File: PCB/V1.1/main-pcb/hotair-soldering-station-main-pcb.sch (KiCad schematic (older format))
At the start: 83 parts, among them J1 230VAC_IN, J10 SOLD_IRON (r.2,54), J13 ICP (goldpin r2,54), J2 main-board-conn, J3 EARTH_GND, J4 24V_IN (NS-25 r2,54), J5 PSUPPLY (PWZ-02S r.3,96), J6 HOTAIR_FAN (JST r,2,54), J7 HOTAIR_MEAS (JST r.2,5), J8 HOTAIR_HEATER (PWZ-02S r.3,96)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

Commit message: Add front panel menu sw, remove lcd, reorganization of uC pinout
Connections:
- net labels added: HOTAIR_FAN_ADC, HOTAIR_FAN_PWM, HOTAIR_TEMP_ADC, IRON_T12_MOTION_SW, IRON_T12_TEMP_ADC, LCD_BACKLIGHT_PWM, LCD_D4, LCD_D5, LCD_D6, LCD_D7, LCD_EN, LCD_RS, LCD_RW, MENU_DOWN_SW, MENU_OK_SW, MENU_UP_SW, SOLDER_SELECT_SW
- net labels removed: 7SEG_LATCH, FAN_ADC, FAN_PWM, HOTAIR_ADC, IRON_T12_ADC
- wire segments 317 -> 324
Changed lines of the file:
@@
 Wire Wire Line
 	20125 2800 20125 2550
+Text GLabel 21150 3200 2    50   Input ~ 0
+HOTAIR_UP_SW
+Text GLabel 21150 3100 2    50   Input ~ 0
+HOTAIR_DOWN_SW
 Text GLabel 20150 3400 0    50   Input ~ 0
-HOTAIR_UP_SW
+SOLDER_UP_SW
 Text GLabel 20150 3300 0    50   Input ~ 0
-HOTAIR_DOWN_SW
-Text GLabel 20150 3200 0    50   Input ~ 0
-SOLDER_UP_SW
-Text GLabel 20150 3100 0    50   Input ~ 0
 SOLDER_DOWN_SW
-Text GLabel 21150 3200 2    50   Input ~ 0
+Text GLabel 21150 2900 2    50   Input ~ 0
 HOTAIR_ON_SW
-Text GLabel 21150 3100 2    50   Input ~ 0
+Text GLabel 21150 2800 2    50   Input ~ 0
 SOLDER_ON_SW
-Text GLabel 21150 2800 2    50   Input ~ 0
-SPI1_MOSI
-Text GLabel 21150 3000 2    50   Input ~ 0
-SPI1_SCK
-Text GLabel 21150 2900 2    50   Input ~ 0
-7SEG_LATCH
 Wire Notes Line
 	6475 11250 6425 11250
@@
 Wire Notes Line
 	12700 16075 12750 16075
-Text GLabel 18450 8950 2    50   Input ~ 0
-HOTAIR_UP_SW
-Text GLabel 16250 8550 0    50   Input ~ 0
-HOTAIR_DOWN_SW
-Text GLabel 18450 8850 2    50   Input ~ 0
-SPI1_MOSI
-Text GLabel 18450 8650 2    50   Input ~ 0
-SPI1_SCK
-Text GLabel 18450 8750 2    50   Input ~ 0
-SPI1_MISO
-Text GLabel 18450 8150 2    50   Input ~ 0
-IRON_T12_ADC
 $Comp
 L Device:R R18
@@
 $EndComp
 Text GLabel 5625 12050 2    50   Input ~ 0
-HOTAIR_ADC
-Text GLabel 18450 8250 2    50   Input ~ 0
-HOTAIR_ADC
+HOTAIR_TEMP_ADC
 Wire Notes Line
 	650  12850 6525 12850
@@
 	1    0    0    -1
 $EndComp
-Text GLabel 18450 9050 2    50   Input ~ 0
+Text GLabel 18450 9650 2    50   Input ~ 0
 UART_DBG_TX
 Wire Wire Line
@@
 	16250 8850 16650 8850
 Wire Wire Line
-	16650 8950 16250 8950
-Wire Wire Line
 	18450 8450 17950 8450
 Wire Wire Line
 	18450 8550 17950 8550
-Text GLabel 16225 8250 0    50   Input ~ 0
-HOTAIR_REED_SW
 Wire Wire Line
 	18450 8950 17950 8950
@@
 FAN_SUPPLY
 Text GLabel 1650 9200 0    50   Input ~ 0
-FAN_PWM
-Text GLabel 18450 9250 2    50   Input ~ 0
-HOTAIR_FAN_DOWN_SW
-Text GLabel 18450 9150 2    50   Input ~ 0
-HOTAIR_FAN_UP_SW
-Wire Wire Line
-	16650 8150 16225 8150
-Wire Wire Line
-	16650 8250 16225 8250
+HOTAIR_FAN_PWM
+Wire Wire Line
+	16650 8150 16250 8150
+Wire Wire Line
+	16650 8250 16250 8250
 $Comp
 L Connector_Generic:Conn_01x06 J9
@@
 $EndComp
 Wire Wire Line
-	20375 2900 19100 2900
-Wire Wire Line
-	19100 2900 19100 3000
-Wire Wire Line
-	20375 3000 19100 3000
-Connection ~ 19100 3000
-Wire Wire Line
-	19100 3000 19100 3425
-Wire Wire Line
 	11100 7025 11425 7025
 $Comp
@@
 Wire Wire Line
 	2225 13850 2225 14025
-Text GLabel 18450 8550 2    50   Input ~ 0
-BUZZER
-Text GLabel 16250 9050 0    50   Input ~ 0
-HOTAIR_HEATER_CTRL
-Text GLabel 16250 8750 0    50   Input ~ 0
-IRON_WEP_HEATER_CTRL
-Wire Wire Line
-	16250 9050 16650 9050
 Wire Wire Line
 	17950 9050 18450 9050
@@
 	1    0    0    -1
 $EndComp
-Text GLabel 16225 8150 0    50   Input ~ 0
-SOLDER_ON_SW
-Text GLabel 16250 8450 0    50   Input ~ 0
-SOLDER_UP_SW
-Text GLabel 18450 9350 2    50   Input ~ 0
-HOTAIR_ON_SW
-Text GLabel 16250 8850 0    50   Input ~ 0
-FAN_PWM
 Text Notes 14275 9375 0    50   ~ 0
 TIM3_CH2 - PWM
@@
 Wire Wire Line
 	14125 11425 14125 11450
-Text GLabel 18450 8450 2    50   Input ~ 0
-FAN_ADC
 Wire Wire Line
 	4525 11575 5225 11575
@@
 	10300 10175 10500 10175
 Text GLabel 11850 10075 2    50   Input ~ 0
-IRON_T12_ADC
+IRON_T12_TEMP_ADC
 $Comp
 L Device:R R16
@@
 	0    -1   1    0
 $EndComp
-Text GLabel 11150 11800 0    50   Input ~ 0
+Text GLabel 11400 11800 0    50   Input ~ 0
 IRON_T12_HEATER
 Text GLabel 11400 12000 0    50   Input ~ 0
@@
 	11400 12000 11625 12000
 Wire Wire Line
-	11150 11800 11500 11800
-Wire Wire Line
-	11625 11900 11500 11900
-Wire Wire Line
-	11500 11900 11500 11800
-Connection ~ 11500 11800
-Wire Wire Line
-	11500 11800 11625 11800
-Wire Wire Line
 	11625 11700 11500 11700
 Wire Wire Line
@@
 Text GLabel 11400 12100 0    50   Input ~ 0
 THERM_GND
-Text GLabel 18450 9650 2    50   Input ~ 0
-MAX31855_HOTAIR_CS
-Text GLabel 16250 8650 0    50   Input ~ 0
-MAX31855_IRON_CS
 $Comp
 L Sensor_Temperature:MAX31855KASA U7
@@
 	3875 9700 3875 9750
 Text GLabel 4325 9700 2    50   Input ~ 0
-FAN_ADC
+HOTAIR_FAN_ADC
 Wire Notes Line
 	725  3250 8700 3250
@@
 	1    0    0    -1
 $EndComp
-Text GLabel 18450 8350 2    50   Input ~ 0
-SOLDER_DOWN_SW
-Text GLabel 16250 8950 0    50   Input ~ 0
-IRON_T12_HEATER_CTRL
 Wire Wire Line
 	18450 9650 17950 9650
@@
 $EndComp
 Wire Wire Line
-	16500 7250 16500 7375
-Wire Wire Line
-	16650 7250 16500 7250
-$Comp
-L power:GND #PWR0116
-U 1 1 5FA8FEE8
-P 16500 7375
-F 0 "#PWR0116" H 16500 7125 50  0001 C CNN
-F 1 "GND" H 16505 7202 50  0000 C CNN
-F 2 "" H 16500 7375 50  0001 C CNN
-F 3 "" H 16500 7375 50  0001 C CNN
-	1    16500 7375
-	1    0    0    -1
-$EndComp
-Wire Wire Line
 	17250 9900 17150 9900
 Wire Wire Line
@@
 	17550 6800 17550 6850
 Connection ~ 17450 6800
+Text GLabel 21150 3000 2    50   Input ~ 0
+SOLDER_SELECT_SW
+Wire Wire Line
+	19100 2900 19100 3425
+Wire Wire Line
+	20375 2900 19100 2900
+Text GLabel 20150 3000 0    50   Input ~ 0
+MENU_UP_SW
+Text GLabel 20150 3100 0    50   Input ~ 0
+MENU_OK_SW
+Text GLabel 20150 3200 0    50   Input ~ 0
+MENU_DOWN_SW
+Wire Wire Line
+	20375 3000 20150 3000
+Text GLabel 16250 9650 0    50   Input ~ 0
+LCD_D7
+Text GLabel 16250 9550 0    50   Input ~ 0
+LCD_D6
+Text GLabel 16250 9450 0    50   Input ~ 0
+LCD_D5
+Text GLabel 16250 9350 0    50   Input ~ 0
+LCD_D4
+Text GLabel 16250 9250 0    50   Input ~ 0
+LCD_EN
+Text GLabel 16250 9150 0    50   Input ~ 0
+LCD_RW
+Text GLabel 16250 9050 0    50   Input ~ 0
+LCD_RS
+Text GLabel 16250 8950 0    50   Input ~ 0
+LCD_BACKLIGHT_PWM
+Wire Wire Line
+	11400 11800 11625 11800
+Text GLabel 11400 11900 0    50   Input ~ 0
+IRON_T12_MOTION_SW
+Wire Wire Line
+	11400 11900 11625 11900
+Text GLabel 10425 18475 0    50   Input ~ 0
+IRON_T12_MOTION_SW
+Wire Wire Line
+	16650 8350 16250 8350
+Wire Wire Line
+	16650 8950 16250 8950
+Wire Wire Line
+	16250 9050 16650 9050
+Wire Wire Line
+	16650 9150 16250 9150
+Wire Wire Line
+	16250 9250 16650 9250
+Wire Wire Line
+	16650 9350 16250 9350
+Wire Wire Line
+	16650 9450 16250 9450
+Wire Wire Line
+	16250 9550 16650 9550
+Wire Wire Line
+	16650 9650 16250 9650
+Text GLabel 14350 7700 0    50   Input ~ 0
+MENU_DOWN_SW
+Text GLabel 14350 7600 0    50   Input ~ 0
+MENU_OK_SW
+Text GLabel 14350 7500 0    50   Input ~ 0
+MENU_UP_SW
+Text GLabel 14375 8100 0    50   Input ~ 0
+SOLDER_SELECT_SW
+Text GLabel 14375 8000 0    50   Input ~ 0
+SOLDER_DOWN_SW
+Text GLabel 14375 8600 0    50   Input ~ 0
+HOTAIR_ON_SW
+Text GLabel 14350 7900 0    50   Input ~ 0
+SOLDER_UP_SW
+Text GLabel 14350 7800 0    50   Input ~ 0
+SOLDER_ON_SW
+Text GLabel 14375 8400 0    50   Input ~ 0
+HOTAIR_FAN_UP_SW
+Text GLabel 14375 8500 0    50   Input ~ 0
+HOTAIR_FAN_DOWN_SW
+Text GLabel 14375 8200 0    50   Input ~ 0
+HOTAIR_DOWN_SW
+Text GLabel 14375 8300 0    50   Input ~ 0
+HOTAIR_UP_SW
+Text GLabel 20075 8225 2    50   Input ~ 0
+IRON_T12_MOTION_SW
+Text GLabel 20075 8325 2    50   Input ~ 0
+IRON_T12_HEATER_CTRL
+Text GLabel 20075 7500 2    50   Input ~ 0
+HOTAIR_FAN_ADC
+Text GLabel 20075 7400 2    50   Input ~ 0
+HOTAIR_FAN_PWM
+Text GLabel 20075 8600 2    50   Input ~ 0
+IRON_WEP_HEATER_CTRL
+Text GLabel 20075 7700 2    50   Input ~ 0
+HOTAIR_HEATER_CTRL
+Text GLabel 20075 7800 2    50   Input ~ 0
+HOTAIR_REED_SW
+Text GLabel 20075 7600 2    50   Input ~ 0
+HOTAIR_TEMP_ADC
+Text GLabel 18450 8550 2    50   Input ~ 0
+BUZZER
+Text GLabel 19775 9725 2    50   Input ~ 0
+MAX31855_IRON_CS
+Text GLabel 19775 9625 2    50   Input ~ 0
+MAX31855_HOTAIR_CS
+Text GLabel 19775 9425 2    50   Input ~ 0
+SPI1_MISO
+Text GLabel 19775 9325 2    50   Input ~ 0
+SPI1_SCK
+Text GLabel 19775 9525 2    50   Input ~ 0
+SPI1_MOSI
+Text GLabel 20075 8125 2    50   Input ~ 0
+IRON_T12_TEMP_ADC
+Wire Wire Line
+	16650 7750 16250 7750
+Wire Wire Line
+	16250 7850 16650 7850
+Wire Wire Line
+	16650 7950 16250 7950
+Wire Wire Line
+	16650 7450 16250 7450
+Wire Wire Line
+	16650 7550 16250 7550
 $EndSCHEMATC

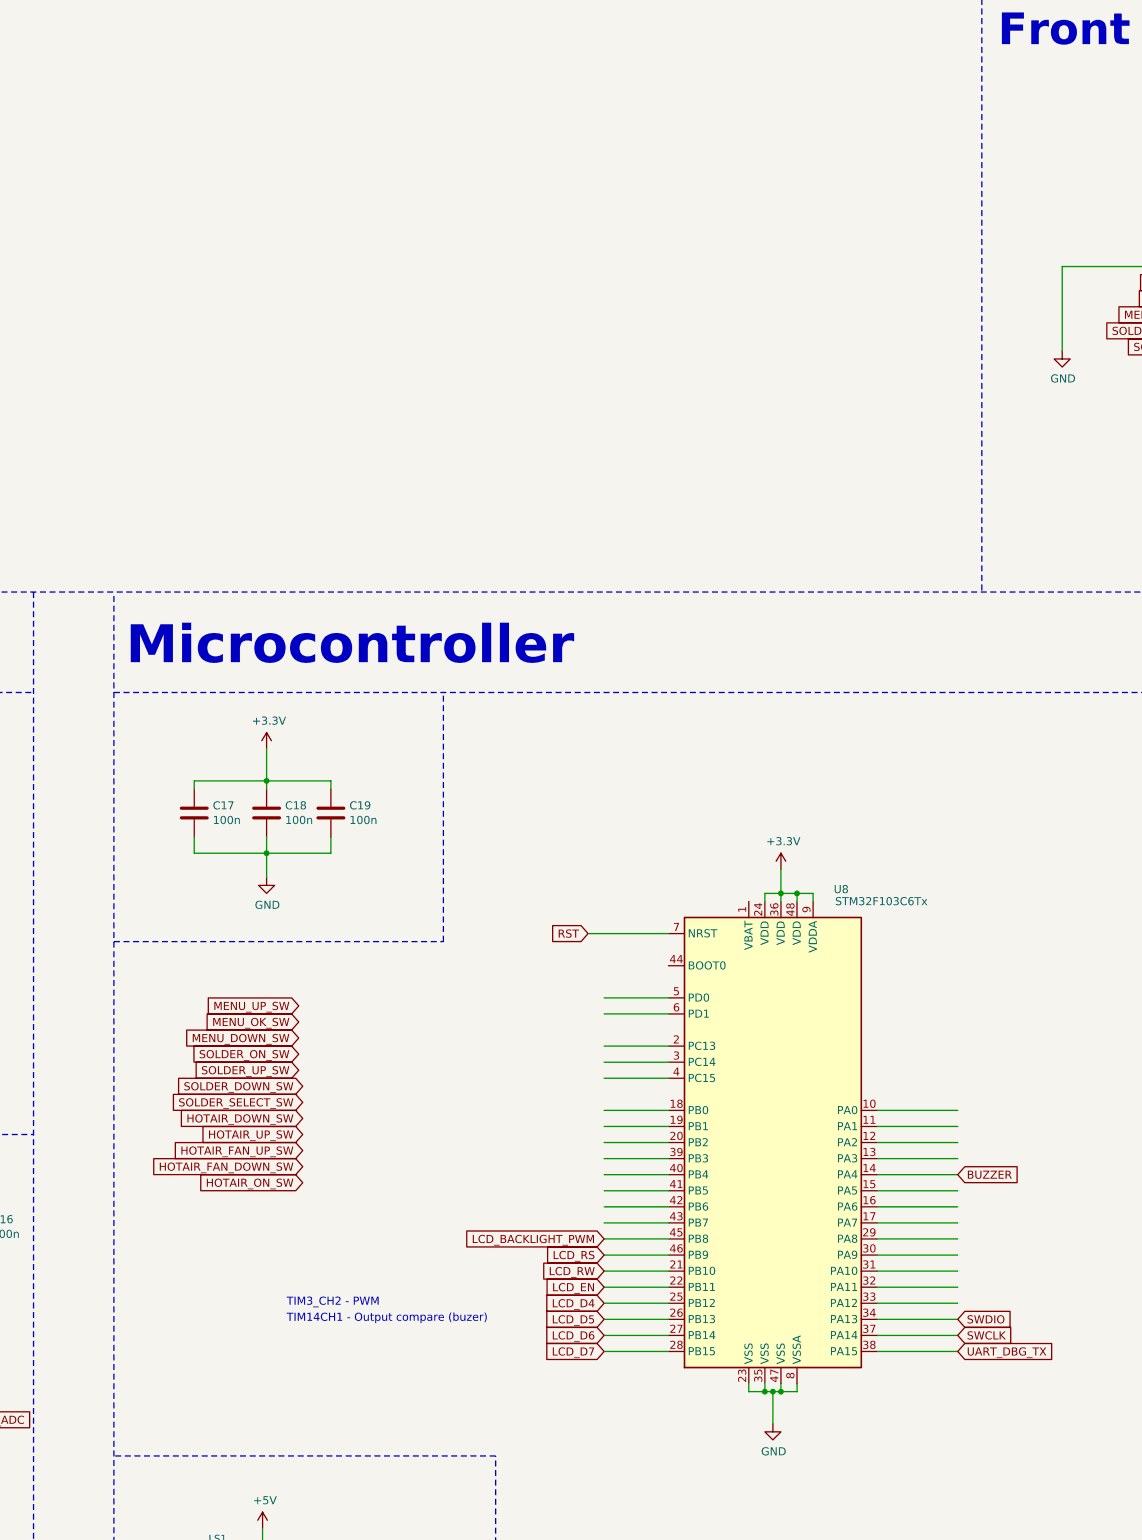
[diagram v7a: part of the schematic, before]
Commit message: LCD connector main pcb
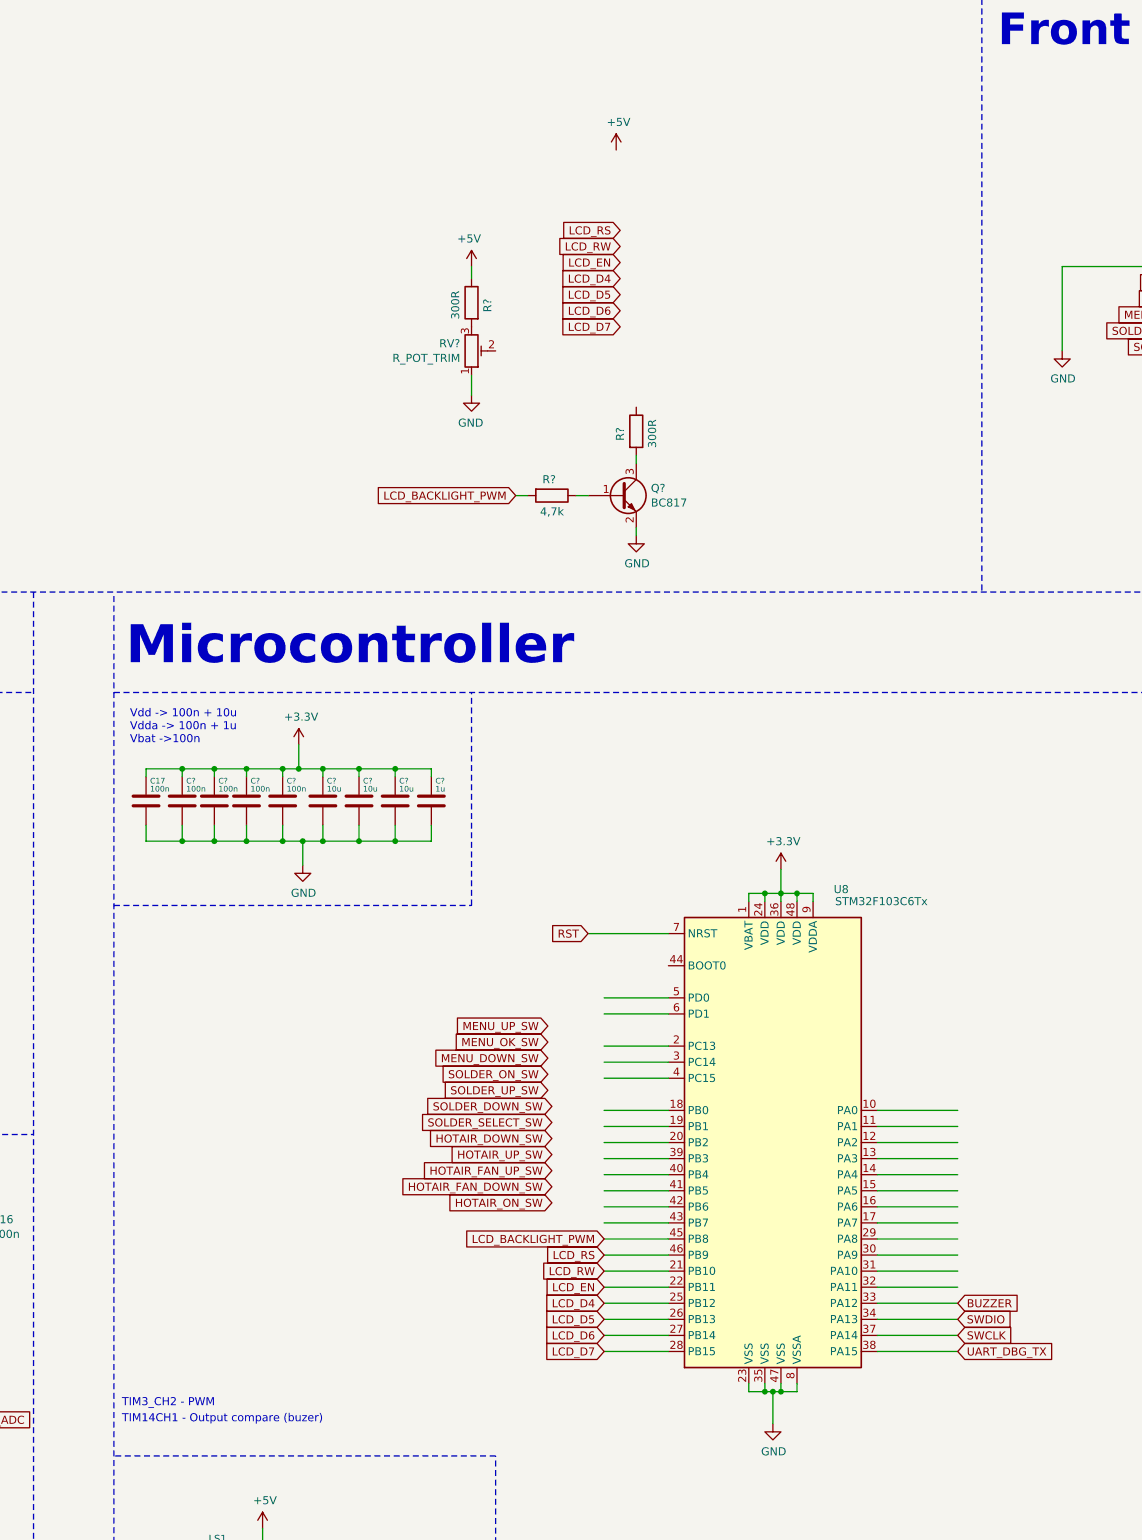
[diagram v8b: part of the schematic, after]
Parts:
- removed C18, C19: 100n, Capacitors:0603, symbol Device:C
- added C? (x4): 100n, Capacitors:0603, symbol Device:C
- added C? (x3): 10u, Capacitors:0603, symbol Device:C
- added C?: 1u, Capacitors:0603, symbol Device:C
- added Q?: BC817, Package_TO_SOT_SMD:SOT-23, symbol Transistor_BJT:BC817
- added R?: 4,7k, Capacitors:0805, symbol Device:R
- added R? (x2): 300R, Capacitors:0805, symbol Device:R
- added RV?: R_POT_TRIM, symbol Device:R_POT_TRIM
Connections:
- wire segments 324 -> 358
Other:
- note added: "Vdd -> 100n + 10u\nVdda -> 100n + 1u\nVbat ->100n"
- moved on the sheet: C17
